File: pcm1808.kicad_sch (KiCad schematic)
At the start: 24 parts, among them J1 ADC IN, U2 PCM1808PWR

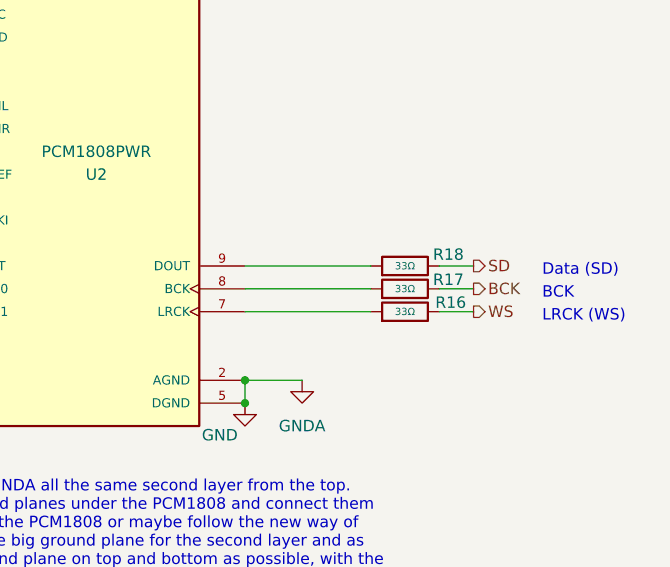
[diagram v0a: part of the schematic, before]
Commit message: Editing 6 layer
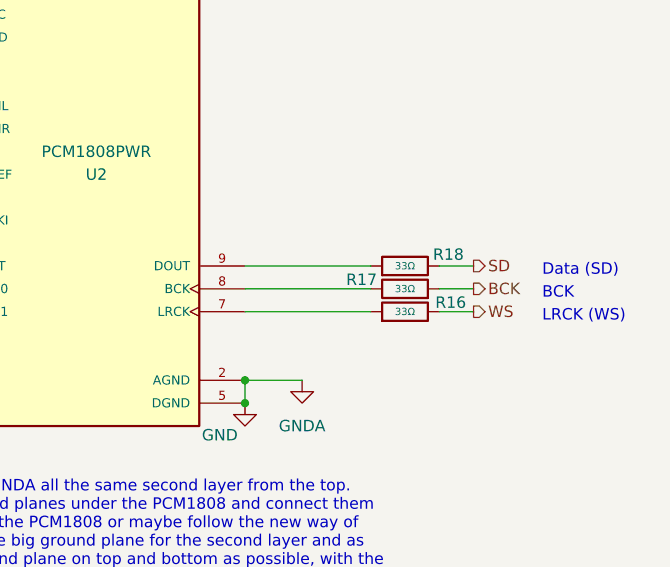
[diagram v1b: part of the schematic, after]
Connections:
- net BCK: now also R17.1; no longer R17.2
- net at U2.8 (BCK): now also R17.2; no longer R17.1
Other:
- moved on the sheet: R17
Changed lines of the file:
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@@
 	(symbol
 		(lib_id "PCM_JLCPCB-Resistors:0805,33Ω")
-		(at 227.33 95.25 90)
+		(at 227.33 95.25 270)
+		(mirror x)
 		(unit 1)
 		(exclude_from_sim no)
@@
 		(dnp no)
 		(property "Reference" "R17"
-			(at 232.156 94.234 90)
+			(at 222.504 94.234 90)
 			(effects
 				(font
